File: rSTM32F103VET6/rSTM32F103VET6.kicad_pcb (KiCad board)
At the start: 2 copper layers, 42.5 x 62.5 mm, 38 parts, among them J1 USB, J2 STLink, J3 BOOT, J4 , J5 , SW1 RESET, U1 STM32F103VET6, U2 RT9013, Y1 CSTCE8.000M, Y2 32.768K

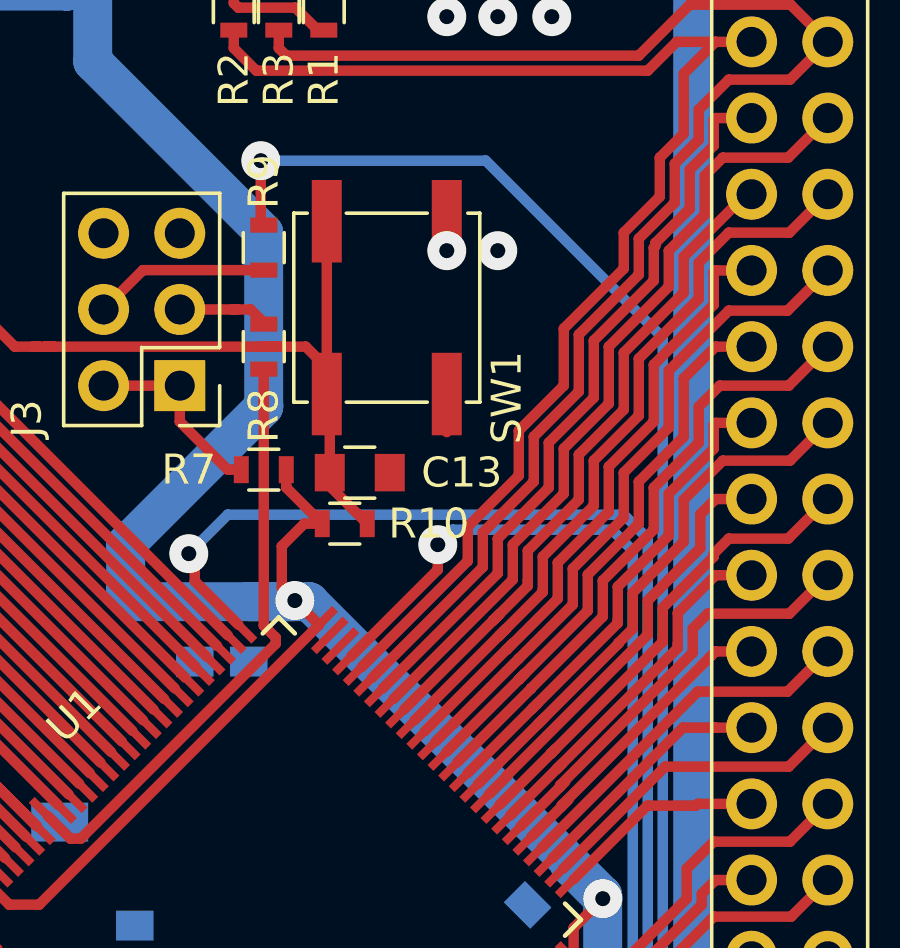
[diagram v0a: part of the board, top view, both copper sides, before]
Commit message: KiCAD Project.
Footprint fix.
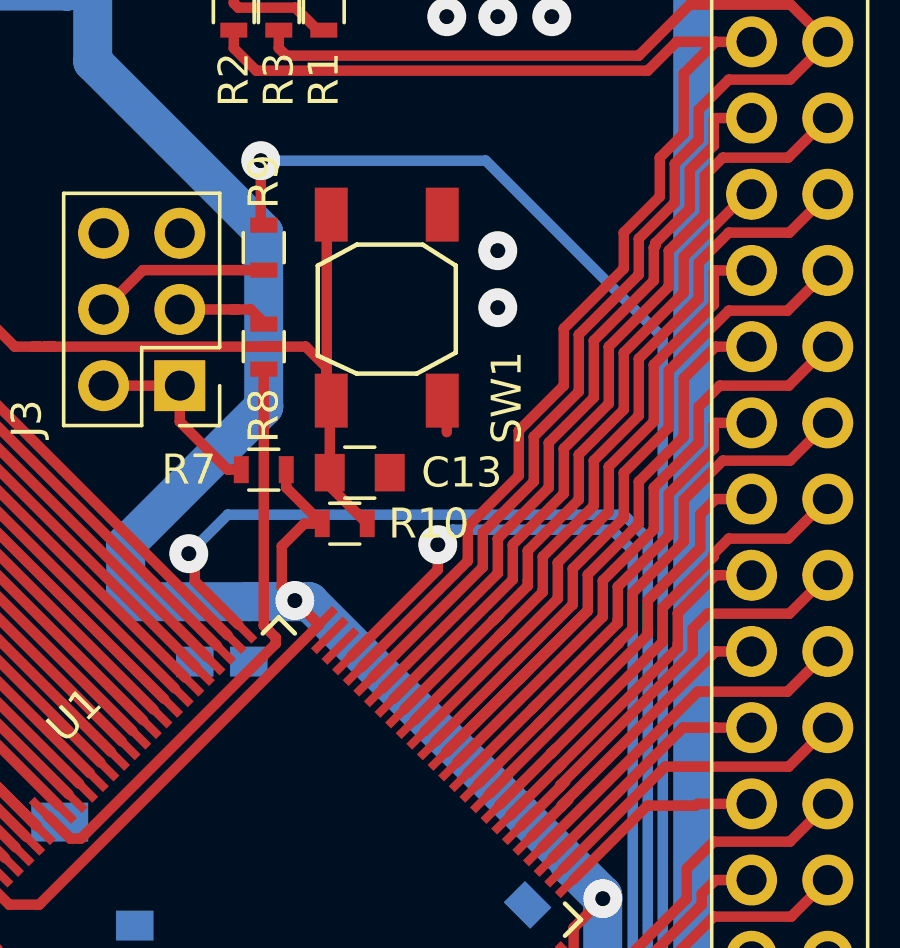
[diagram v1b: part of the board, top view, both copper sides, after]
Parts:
- SW1: footprint Buttons_Switches_SMD:SW_SPST_EVPBF -> .rpvM:Switch_SMD_5.2x6.4_reset
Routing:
- net /PC6: track 18.7 -> 25.4 mm
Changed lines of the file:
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@@
     (thickness 1.6)
     (drawings 4)
-    (tracks 782)
+    (tracks 779)
     (zones 0)
     (modules 38)
@@
       (effects (font (size 1 1) (thickness 0.15)) (justify mirror))
     )
+    (fp_line (start -1.9 2) (end 1.9 2) (layer B.SilkS) (width 0.15))
+    (fp_line (start -1.9 -2) (end 1.9 -2) (layer B.SilkS) (width 0.15))
+    (fp_line (start 4 -2) (end 3.6 -2) (layer B.SilkS) (width 0.15))
+    (fp_line (start 4 2) (end 3.6 2) (layer B.SilkS) (width 0.15))
+    (fp_line (start -4 2) (end -3.6 2) (layer B.SilkS) (width 0.15))
+    (fp_line (start -4 -2) (end -3.6 -2) (layer B.SilkS) (width 0.15))
     (fp_arc (start -4 0) (end -4 -0.6) (angle 180) (layer B.SilkS) (width 0.15))
     (fp_circle (center 3.1 0) (end 3.5 -0.1) (layer B.SilkS) (width 0.15))
     (fp_line (start -4 -2) (end -4 2) (layer B.SilkS) (width 0.15))
-    (fp_line (start 4 -2) (end -4 -2) (layer B.SilkS) (width 0.15))
     (fp_line (start 4 2) (end 4 -2) (layer B.SilkS) (width 0.15))
-    (fp_line (start -4 2) (end 4 2) (layer B.SilkS) (width 0.15))
     (pad 4 smd rect (at -2.75 1.6 90) (size 1.3 1.9) (layers B.Cu B.Paste B.Mask)
       (net 8 /PC15))
@@
     (pad 1 smd rect (at -2.75 -1.6 90) (size 1.3 1.9) (layers B.Cu B.Paste B.Mask)
       (net 7 /PC14))
+  )
+  (module .rpvM:Switch_SMD_5.2x6.4_reset (layer F.Cu)
+    (at 69.3 50.6 90)
+    (fp_text reference SW1 (at -3 4 90) (layer F.SilkS)
+      (effects (font (size 1 1) (thickness 0.15)))
+    )
+    (fp_text value RESET (at 2.3 4 90) (layer F.Fab)
+      (effects (font (size 1 1) (thickness 0.15)))
+    )
+    (fp_line (start -2.2 -1) (end -1.6 -2.3) (layer F.SilkS) (width 0.15))
+    (fp_line (start -1.5 2.3) (end -2.2 1) (layer F.SilkS) (width 0.15))
+    (fp_line (start 1.4 2.3) (end 2.1 1.2) (layer F.SilkS) (width 0.15))
+    (fp_line (start 2.1 -1) (end 1.4 -2.3) (layer F.SilkS) (width 0.15))
+    (fp_line (start -1.6 -2.3) (end 1.4 -2.3) (layer F.SilkS) (width 0.15))
+    (fp_line (start 2.1 1.2) (end 2.1 -1) (layer F.SilkS) (width 0.15))
+    (fp_line (start -1.5 2.3) (end 1.4 2.3) (layer F.SilkS) (width 0.15))
+    (fp_line (start -2.2 -1) (end -2.2 1) (layer F.SilkS) (width 0.15))
+    (fp_text user %R (at -3 4 90) (layer F.Fab)
+      (effects (font (size 1 1) (thickness 0.15)))
+    )
+    (pad 1 smd rect (at 3.1 -1.85 90) (size 1.8 1.1) (layers F.Cu F.Paste F.Mask)
+      (net 9 /NRST))
+    (pad 2 smd rect (at 3.1 1.85 90) (size 1.8 1.1) (layers F.Cu F.Paste F.Mask)
+      (net 1 GND))
+    (pad 2 smd rect (at -3.1 1.85 90) (size 1.8 1.1) (layers F.Cu F.Paste F.Mask)
+      (net 1 GND))
+    (pad 1 smd rect (at -3.1 -1.85 90) (size 1.8 1.1) (layers F.Cu F.Paste F.Mask)
+      (net 9 /NRST))
   )
   (module Pin_Headers:Pin_Header_Straight_2x22_Pitch2.54mm (layer F.Cu)
@@
     )
   )
-  (module Buttons_Switches_SMD:SW_SPST_EVPBF (layer F.Cu)
-    (at 69.3 50.6 90)
-    (descr "Light Touch Switch")
-    (attr smd)
-    (fp_text reference SW1 (at -3 4 90) (layer F.SilkS)
-      (effects (font (size 1 1) (thickness 0.15)))
-    )
-    (fp_text value RESET (at 2.3 4 90) (layer F.Fab)
-      (effects (font (size 1 1) (thickness 0.15)))
-    )
-    (fp_circle (center 0 0) (end 1.7 0) (layer F.Fab) (width 0.1))
-    (fp_line (start -4.5 3.25) (end -4.5 -3.25) (layer F.CrtYd) (width 0.05))
-    (fp_line (start 4.5 3.25) (end -4.5 3.25) (layer F.CrtYd) (width 0.05))
-    (fp_line (start 4.5 -3.25) (end 4.5 3.25) (layer F.CrtYd) (width 0.05))
-    (fp_line (start -4.5 -3.25) (end 4.5 -3.25) (layer F.CrtYd) (width 0.05))
-    (fp_text user %R (at -3 4 90) (layer F.Fab)
-      (effects (font (size 1 1) (thickness 0.15)))
-    )
-    (fp_line (start -3 3) (end -3 -3) (layer F.Fab) (width 0.1))
-    (fp_line (start 3 3) (end -3 3) (layer F.Fab) (width 0.1))
-    (fp_line (start 3 -3) (end 3 3) (layer F.Fab) (width 0.1))
-    (fp_line (start -3 -3) (end 3 -3) (layer F.Fab) (width 0.1))
-    (fp_line (start -3.15 -2.65) (end -3.15 -3.1) (layer F.SilkS) (width 0.12))
-    (fp_line (start 3.15 -3.1) (end 3.15 -2.65) (layer F.SilkS) (width 0.12))
-    (fp_line (start -3.15 -3.1) (end 3.15 -3.1) (layer F.SilkS) (width 0.12))
-    (fp_line (start 3.15 -1.35) (end 3.15 1.35) (layer F.SilkS) (width 0.12))
-    (fp_line (start -3.15 1.35) (end -3.15 -1.35) (layer F.SilkS) (width 0.12))
-    (fp_line (start 3.15 3.1) (end 3.15 2.7) (layer F.SilkS) (width 0.12))
-    (fp_line (start -3.15 3.1) (end 3.15 3.1) (layer F.SilkS) (width 0.12))
-    (fp_line (start -3.15 2.65) (end -3.15 3.1) (layer F.SilkS) (width 0.12))
-    (pad 2 smd rect (at 2.88 2 90) (size 2.75 1) (layers F.Cu F.Paste F.Mask)
-      (net 1 GND))
-    (pad 2 smd rect (at -2.88 2 90) (size 2.75 1) (layers F.Cu F.Paste F.Mask)
-      (net 1 GND))
-    (pad 1 smd rect (at -2.88 -2 90) (size 2.75 1) (layers F.Cu F.Paste F.Mask)
-      (net 9 /NRST))
-    (pad 1 smd rect (at 2.88 -2 90) (size 2.75 1) (layers F.Cu F.Paste F.Mask)
-      (net 9 /NRST))
-    (model ${KISYS3DMOD}/Buttons_Switches_SMD.3dshapes/SW_SPST_EVPBF.wrl
-      (at (xyz 0 0 0))
-      (scale (xyz 1 1 1))
-      (rotate (xyz 0 0 0))
-    )
-  )
   (module Housings_QFP:LQFP-100_14x14mm_Pitch0.5mm (layer F.Cu)
     (at 65.7 71 45)
@@
   (gr_line (start 87 30.5) (end 87 93) (layer Edge.Cuts) (width 0.05))
   (gr_line (start 44.5 30.5) (end 87 30.5) (layer Edge.Cuts) (width 0.05))
-  (via (at 71.3 48.7) (size 1.3) (drill 0.5) (layers F.Cu B.Cu) (net 1))
+  (via (at 73 50.6) (size 1.3) (drill 0.5) (layers F.Cu B.Cu) (net 1))
   (segment (start 52.7 77.6) (end 52.575 77.6) (width 0.35) (layer F.Cu) (net 1))
   (segment (start 71.3 53.48) (end 71.3 54.75) (width 0.35) (layer F.Cu) (net 1))
@@
   (segment (start 77.2 56.1) (end 78.7 54.6) (width 0.35) (layer F.Cu) (net 62))
   (segment (start 75.5 59.3) (end 77.2 57.6) (width 0.35) (layer F.Cu) (net 62))
-  (segment (start 70.93259 65.060303) (end 71.53363 64.459263) (width 0.35) (layer F.Cu) (net 62))
-  (segment (start 71.540737 64.459263) (end 73.7 62.3) (width 0.35) (layer F.Cu) (net 62))
-  (segment (start 71.53363 64.459263) (end 71.540737 64.459263) (width 0.35) (layer F.Cu) (net 62))
   (segment (start 78.7 54.6) (end 78.7 52.7) (width 0.35) (layer F.Cu) (net 62))
   (segment (start 77.2 57.6) (end 77.2 56.1) (width 0.35) (layer F.Cu) (net 62))
   (segment (start 82.66 50.7) (end 84 49.36) (width 0.35) (layer F.Cu) (net 62))
-  (segment (start 73.7 62.3) (end 75.5 60.5) (width 0.35) (layer F.Cu) (net 62))
   (segment (start 75.5 60.5) (end 75.5 59.3) (width 0.35) (layer F.Cu) (net 62))
+  (segment (start 75.492893 60.5) (end 75.5 60.5) (width 0.35) (layer F.Cu) (net 62))
+  (segment (start 70.93259 65.060303) (end 75.492893 60.5) (width 0.35) (layer F.Cu) (net 62))
   (segment (start 79.2 52.957919) (end 80.257919 51.9) (width 0.35) (layer F.Cu) (net 63))
   (segment (start 80.257919 51.9) (end 81.46 51.9) (width 0.35) (layer F.Cu) (net 63))
@@
   (segment (start 73.7 63) (end 73.9 62.8) (width 0.35) (layer F.Cu) (net 63))
   (segment (start 71.286144 65.413856) (end 73.7 63) (width 0.35) (layer F.Cu) (net 63))
-  (segment (start 71.639697 65.76741) (end 74.107107 63.3) (width 0.35) (layer F.Cu) (net 64))
+  (segment (start 71.286144 65.413856) (end 76 60.7) (width 0.35) (layer F.Cu) (net 63))
+  (segment (start 82.7 53.2) (end 84 51.9) (width 0.35) (layer F.Cu) (net 64))
+  (segment (start 80.4 53.2) (end 82.7 53.2) (width 0.35) (layer F.Cu) (net 64))
+  (segment (start 79.7 53.9) (end 80.4 53.2) (width 0.35) (layer F.Cu) (net 64))
+  (segment (start 76.5 60.907107) (end 76.5 59.7) (width 0.35) (layer F.Cu) (net 64))
+  (segment (start 71.639697 65.76741) (end 76.5 60.907107) (width 0.35) (layer F.Cu) (net 64))
   (segment (start 76.5 59.7) (end 78.2 58) (width 0.35) (layer F.Cu) (net 64))
   (segment (start 78.2 58) (end 78.2 56.6) (width 0.35) (layer F.Cu) (net 64))
   (segment (start 78.2 56.6) (end 79.7 55.1) (width 0.35) (layer F.Cu) (net 64))
   (segment (start 79.7 55.1) (end 79.7 53.9) (width 0.35) (layer F.Cu) (net 64))
-  (segment (start 79.7 53.9) (end 80.4 53.2) (width 0.35) (layer F.Cu) (net 64))
-  (segment (start 82.7 53.2) (end 84 51.9) (width 0.35) (layer F.Cu) (net 64))
-  (segment (start 80.4 53.2) (end 82.7 53.2) (width 0.35) (layer F.Cu) (net 64))
-  (segment (start 74.107107 63.292893) (end 76.5 60.9) (width 0.35) (layer F.Cu) (net 64))
-  (segment (start 74.107107 63.3) (end 74.107107 63.292893) (width 0.35) (layer F.Cu) (net 64))
-  (segment (start 76.5 60.9) (end 76.5 59.7) (width 0.35) (layer F.Cu) (net 64))
   (segment (start 80.257919 54.44) (end 81.46 54.44) (width 0.35) (layer F.Cu) (net 65))
   (segment (start 80.2 54.497919) (end 80.257919 54.44) (width 0.35) (layer F.Cu) (net 65))
